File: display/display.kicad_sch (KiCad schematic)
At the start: 19 parts, among them J1 DIN41612_03x32_ABC

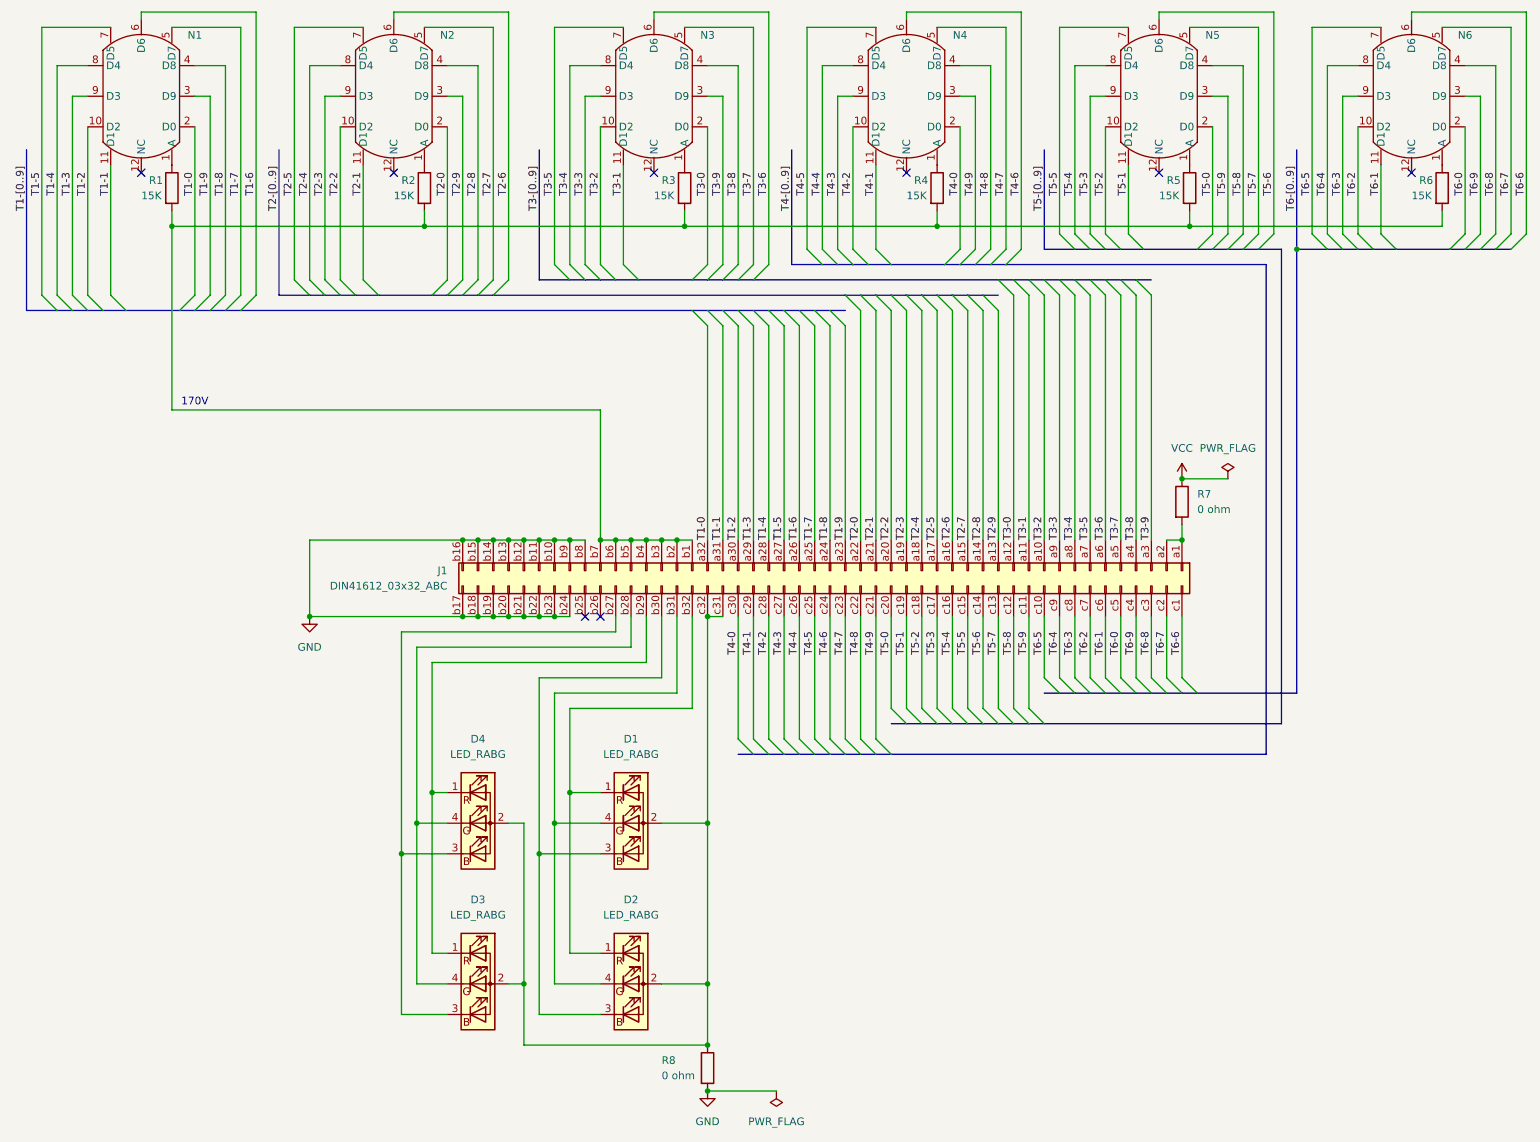
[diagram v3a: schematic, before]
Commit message: Clean up symbol library references to be local to repo
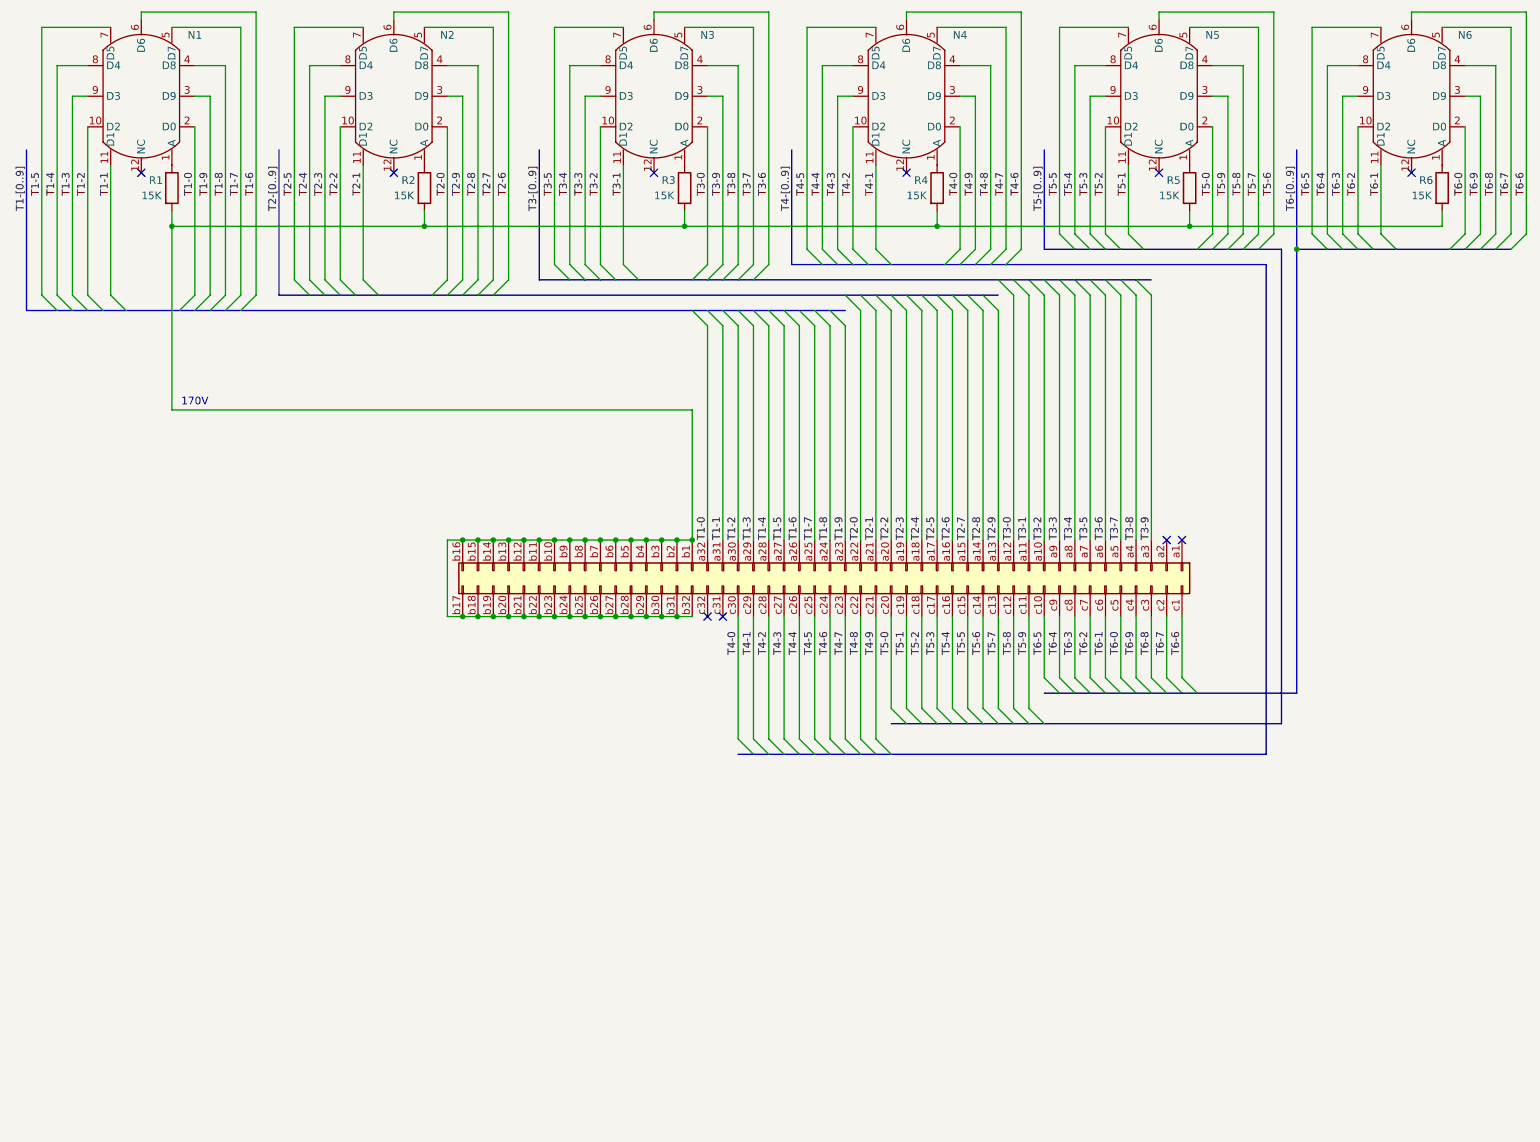
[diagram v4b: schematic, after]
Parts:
- removed D1, D2, D3, D4: LED_RABG, LED_THT:LED_D5.0mm-4_RGB, symbol Device:LED_RABG
- removed R7, R8: 0 ohm, Resistor_THT:R_Box_L14.0mm_W5.0mm_P9.00mm, symbol Device:R
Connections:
- net GND is gone; now on an unnamed net: J1.b10 (Pin_b10), J1.b11 (Pin_b11), J1.b12 (Pin_b12), J1.b13 (Pin_b13), J1.b14 (Pin_b14), J1.b15 (Pin_b15), J1.b16 (Pin_b16), J1.b17 (Pin_b17), J1.b18 (Pin_b18), J1.b19 (Pin_b19), J1.b20 (Pin_b20), J1.b21 (Pin_b21), J1.b22 (Pin_b22), J1.b23 (Pin_b23), J1.b24 (Pin_b24), J1.b8 (Pin_b8), J1.b9 (Pin_b9)
- net at J1.b1 (Pin_b1), J1.b2 (Pin_b2), J1.b3 (Pin_b3)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: now also J1.b25 (Pin_b25), J1.b26 (Pin_b26), J1.b27 (Pin_b27), J1.b28 (Pin_b28), J1.b29 (Pin_b29), J1.b30 (Pin_b30), J1.b31 (Pin_b31), J1.b32 (Pin_b32)
- net at J1.a1 (Pin_a1): no longer J1.a2 (Pin_a2)
- net at J1.c31 (Pin_c31): no longer J1.c32 (Pin_c32)
- no-connect marks 8 -> 10

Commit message: Add Nixie socket to NixComp lib and update PCB
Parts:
- N1, N2, N3, N4, N5, N6: footprint hatsunearu:IN_12B_Socket -> NixComp:IN_12B_Socket
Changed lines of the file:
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@@
 			)
 		)
-		(property "Footprint" "hatsunearu:IN_12B_Socket"
+		(property "Footprint" "NixComp:IN_12B_Socket"
 			(at 246.38 31.75 0)
 			(effects
@@
 			)
 		)
-		(property "Footprint" "hatsunearu:IN_12B_Socket"
+		(property "Footprint" "NixComp:IN_12B_Socket"
 			(at 162.56 31.75 0)
 			(effects
@@
 			)
 		)
-		(property "Footprint" "hatsunearu:IN_12B_Socket"
+		(property "Footprint" "NixComp:IN_12B_Socket"
 			(at 77.47 31.75 0)
 			(effects
@@
 			)
 		)
-		(property "Footprint" "hatsunearu:IN_12B_Socket"
+		(property "Footprint" "NixComp:IN_12B_Socket"
 			(at 35.56 31.75 0)
 			(effects
@@
 			)
 		)
-		(property "Footprint" "hatsunearu:IN_12B_Socket"
+		(property "Footprint" "NixComp:IN_12B_Socket"
 			(at 120.65 31.75 0)
 			(effects
@@
 			)
 		)
-		(property "Footprint" "hatsunearu:IN_12B_Socket"
+		(property "Footprint" "NixComp:IN_12B_Socket"
 			(at 204.47 31.75 0)
 			(effects

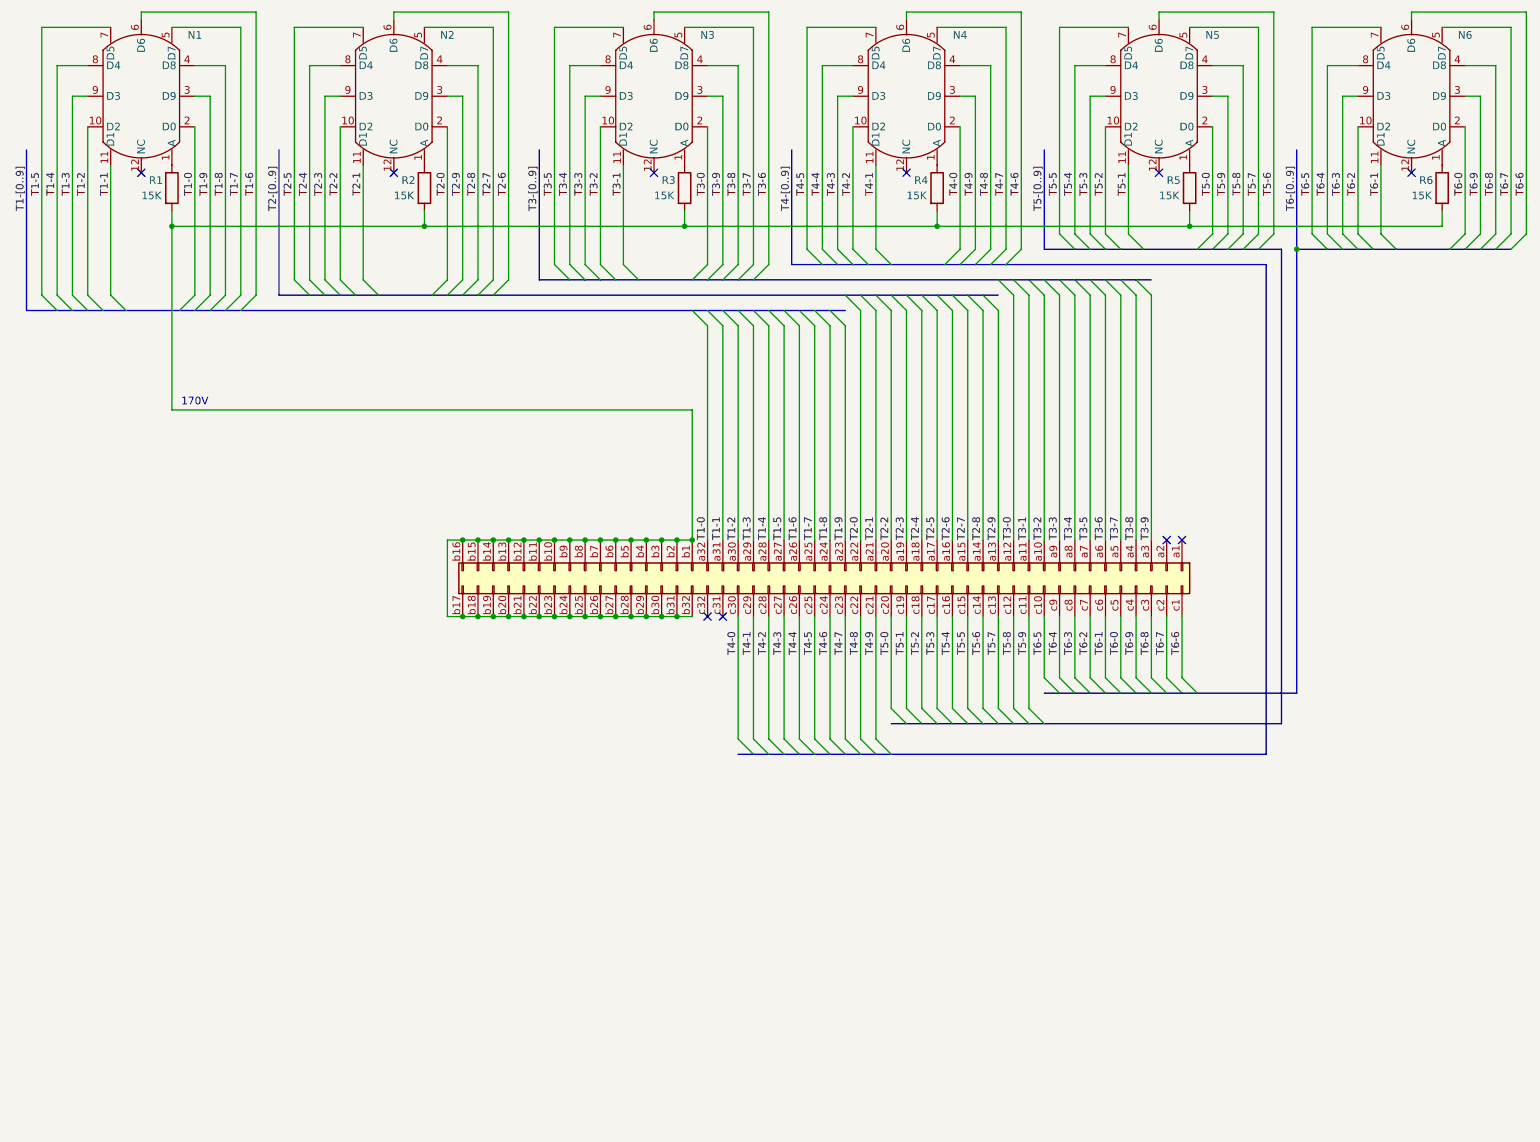
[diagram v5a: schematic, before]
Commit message: Ongoing development. Add shunt resistors to display board.
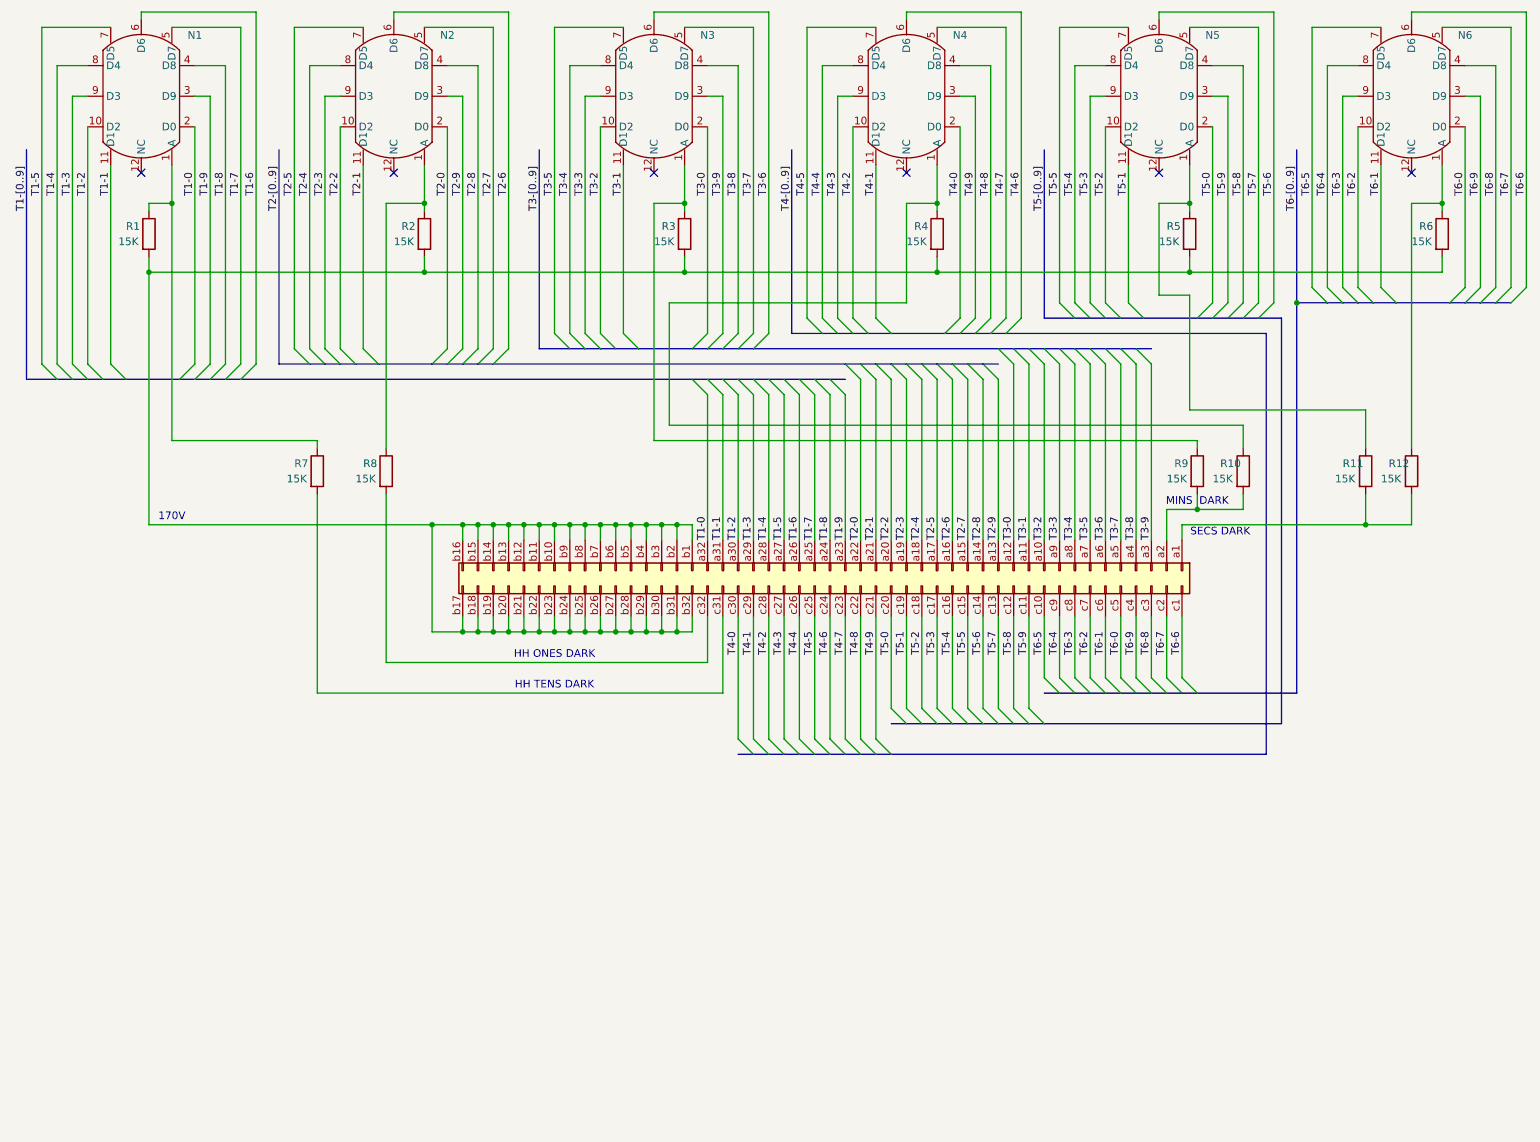
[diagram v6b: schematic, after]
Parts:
- added R10, R11, R12, R7, R8, R9: 15K, Resistor_THT:R_Box_L14.0mm_W5.0mm_P9.00mm, symbol Device:R
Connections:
- net at N6.1 (A), R6.1: now also R12.1
- net at N4.1 (A), R4.1: now also R10.1
- net at J1.a1 (Pin_a1): now also R11.2, R12.2
- net at J1.a2 (Pin_a2): now also R10.2, R9.2
- net at J1.c31 (Pin_c31): now also R7.2
- net at J1.c32 (Pin_c32): now also R8.2
- net at N3.1 (A), R3.1: now also R9.1
- net at N1.1 (A), R1.1: now also R7.1
- net at N5.1 (A), R5.1: now also R11.1
- net at N2.1 (A), R2.1: now also R8.1
- no-connect marks 10 -> 6
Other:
- note added: "HH ONES DARK"
- note added: "HH TENS DARK"
- note added: "MINS DARK"
- note added: "SECS DARK"
- moved on the sheet: R1, R2, R3, R4, R5, R6

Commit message: Ongoing development
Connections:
- net T4-0: now also J1.c25 (Pin_c25); no longer J1.c30 (Pin_c30)
- net T4-1: now also J1.c26 (Pin_c26); no longer J1.c29 (Pin_c29)
- net T4-2: now also J1.c27 (Pin_c27); no longer J1.c28 (Pin_c28)
- net T4-3: now also J1.c28 (Pin_c28); no longer J1.c27 (Pin_c27)
- net T4-4: now also J1.c29 (Pin_c29); no longer J1.c26 (Pin_c26)
- net T4-5: now also J1.c30 (Pin_c30); no longer J1.c25 (Pin_c25)
- net T4-6: now also J1.c21 (Pin_c21); no longer J1.c24 (Pin_c24)
- net T4-7: now also J1.c22 (Pin_c22); no longer J1.c23 (Pin_c23)
- net T4-8: now also J1.c23 (Pin_c23); no longer J1.c22 (Pin_c22)
- net T4-9: now also J1.c24 (Pin_c24); no longer J1.c21 (Pin_c21)
- net T5-0: now also J1.c15 (Pin_c15); no longer J1.c20 (Pin_c20)
- net T5-1: now also J1.c16 (Pin_c16); no longer J1.c19 (Pin_c19)
- net T5-2: now also J1.c17 (Pin_c17); no longer J1.c18 (Pin_c18)
- net T5-3: now also J1.c18 (Pin_c18); no longer J1.c17 (Pin_c17)
- net T5-4: now also J1.c19 (Pin_c19); no longer J1.c16 (Pin_c16)
- net T5-5: now also J1.c20 (Pin_c20); no longer J1.c15 (Pin_c15)
- net T5-6: now also J1.c11 (Pin_c11); no longer J1.c14 (Pin_c14)
- net T5-7: now also J1.c12 (Pin_c12); no longer J1.c13 (Pin_c13)
- net T5-8: now also J1.c13 (Pin_c13); no longer J1.c12 (Pin_c12)
- net T5-9: now also J1.c14 (Pin_c14); no longer J1.c11 (Pin_c11)
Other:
- note added: "HOUR ONES DARK"
- note added: "HOUR TENS DARK"
- note removed: "HH ONES DARK"
- note removed: "HH TENS DARK"
- moved on the sheet: R11, R7, R8
